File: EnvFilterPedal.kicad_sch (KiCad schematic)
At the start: 114 parts, among them J101 ScopeGroundLoop, J102 IO, Q101 BC857, Q102 BC857, Q103 BC847, U101 TL074, U102 TL074, U103 TL074, U104 LM13700, U105 AZ34063U

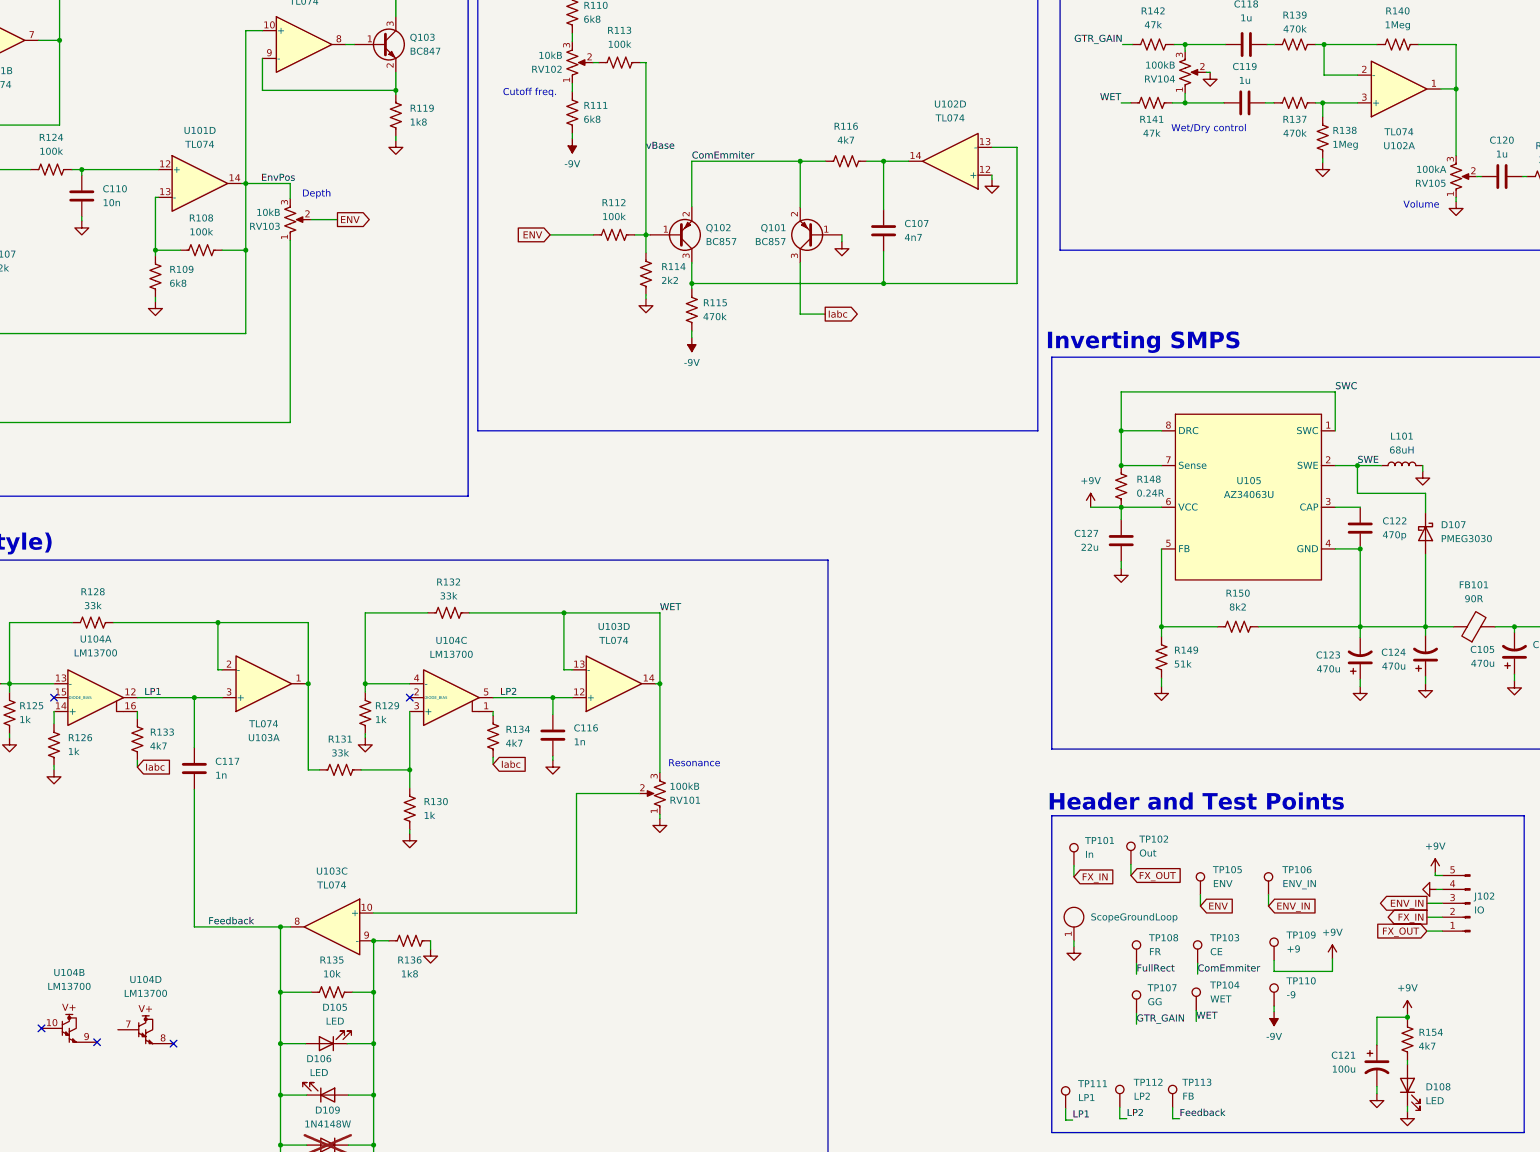
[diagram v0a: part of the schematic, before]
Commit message: component tweaks after playing thru it for a day
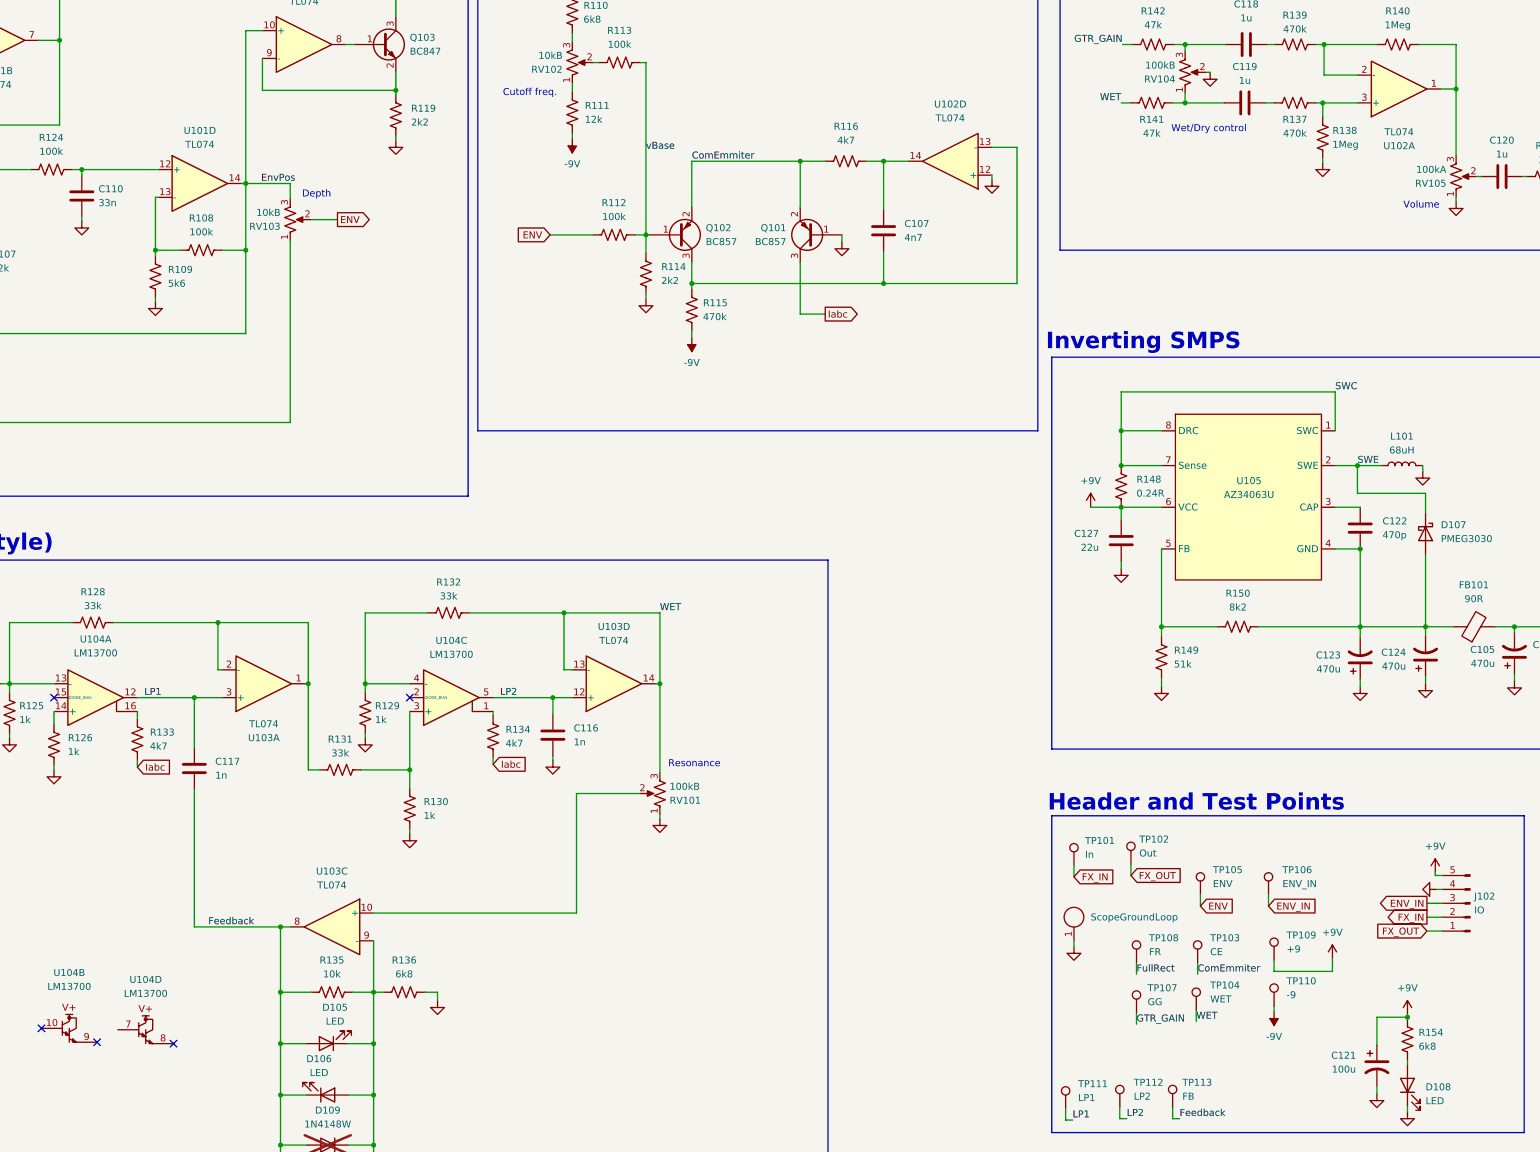
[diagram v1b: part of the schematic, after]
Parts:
- C110: value 10n -> 33n
- R109: value 6k8 -> 5k6
- R111: value 6k8 -> 12k
- R119: value 1k8 -> 2k2
- R136: value 1k8 -> 6k8
- R154: value 4k7 -> 6k8
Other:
- moved on the sheet: R136
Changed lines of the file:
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@@
 	)
 	(junction
-		(at 164.592 214.884)
-		(diameter 0)
-		(color 0 0 0 0)
-	)
-	(junction
 		(at 338.074 61.722)
 		(diameter 0)
@@
 	(wire
 		(pts
+			(xy 164.592 224.282) (xy 166.37 224.282)
+		)
+		(stroke
+			(width 0)
+			(type default)
+		)
+	)
+	(wire
+		(pts
 			(xy 163.068 167.894) (xy 163.068 169.418)
 		)
@@
 	(wire
 		(pts
-			(xy 175.006 214.884) (xy 175.006 216.408)
+			(xy 176.276 224.282) (xy 176.276 225.806)
 		)
 		(stroke
@@
 	(wire
 		(pts
+			(xy 176.276 224.282) (xy 173.99 224.282)
+		)
+		(stroke
+			(width 0)
+			(type default)
+		)
+	)
+	(wire
+		(pts
 			(xy 152.654 261.366) (xy 147.574 261.366)
 		)
@@
 	(wire
 		(pts
-			(xy 164.592 214.884) (xy 167.386 214.884)
-		)
-		(stroke
-			(width 0)
-			(type default)
-		)
-	)
-	(wire
-		(pts
 			(xy 327.914 51.054) (xy 329.184 51.054)
 		)
@@
 			)
 		)
-		(property "Value" "4k7"
+		(property "Value" "6k8"
 			(at 355.6 234.1879 0)
 			(effects
@@
 		(fields_autoplaced yes)
 		(property "Reference" "R119"
-			(at 171.196 62.7379 0)
+			(at 171.45 62.7379 0)
 			(effects
 				(font
@@
 			)
 		)
-		(property "Value" "1k8"
-			(at 171.196 65.2779 0)
+		(property "Value" "2k2"
+			(at 171.45 65.2779 0)
 			(effects
 				(font
@@
 		(fields_autoplaced yes)
 		(property "Reference" "R109"
-			(at 127.254 92.2019 0)
+			(at 127 92.2019 0)
 			(effects
 				(font
@@
 			)
 		)
-		(property "Value" "6k8"
-			(at 127.254 94.7419 0)
+		(property "Value" "5k6"
+			(at 127 94.7419 0)
 			(effects
 				(font
@@
 		(fields_autoplaced yes)
 		(property "Reference" "C110"
-			(at 115.062 77.4699 0)
+			(at 114.3 77.4699 0)
 			(effects
 				(font
@@
 			)
 		)
-		(property "Value" "10n"
-			(at 115.062 80.0099 0)
+		(property "Value" "33n"
+			(at 114.3 80.0099 0)
 			(effects
 				(font
@@
 	(symbol
 		(lib_id "Device:R_US")
-		(at 171.196 214.884 270)
+		(at 170.18 224.282 270)
 		(unit 1)
 		(exclude_from_sim no)
@@
 		(fields_autoplaced yes)
 		(property "Reference" "R136"
-			(at 171.196 218.44 90)
+			(at 170.18 218.44 90)
 			(effects
 				(font
@@
 			)
 		)
-		(property "Value" "1k8"
-			(at 171.196 220.98 90)
+		(property "Value" "6k8"
+			(at 170.18 220.98 90)
 			(effects
 				(font
@@
 		)
 		(property "Footprint" "Resistor_SMD:R_0805_2012Metric"
-			(at 170.942 215.9 90)
+			(at 169.926 225.298 90)
 			(effects
 				(font
@@
 		)
 		(property "Datasheet" "~"
-			(at 171.196 214.884 0)
+			(at 170.18 224.282 0)
 			(effects
 				(font
@@
 		)
 		(property "Description" "Resistor, US symbol"
-			(at 171.196 214.884 0)
+			(at 170.18 224.282 0)
 			(effects
 				(font
@@
 		(fields_autoplaced yes)
 		(property "Reference" "R111"
-			(at 202.946 62.2299 0)
+			(at 203.2 62.2299 0)
 			(effects
 				(font
@@
 			)
 		)
-		(property "Value" "6k8"
-			(at 202.946 64.7699 0)
+		(property "Value" "12k"
+			(at 203.2 64.7699 0)
 			(effects
 				(font
@@
 	(symbol
 		(lib_id "power:GND")
-		(at 175.006 216.408 0)
+		(at 176.276 225.806 0)
 		(mirror y)
 		(unit 1)
@@
 		(fields_autoplaced yes)
 		(property "Reference" "#PWR0141"
-			(at 175.006 222.758 0)
+			(at 176.276 232.156 0)
 			(effects
 				(font
@@
 		)
 		(property "Value" "GND"
-			(at 175.006 220.218 0)
+			(at 176.276 229.616 0)
 			(effects
 				(font
@@
 		)
 		(property "Footprint" ""
-			(at 175.006 216.408 0)
+			(at 176.276 225.806 0)
 			(effects
 				(font
@@
 		)
 		(property "Datasheet" ""
-			(at 175.006 216.408 0)
+			(at 176.276 225.806 0)
 			(effects
 				(font
@@
 		)
 		(property "Description" "Power symbol creates a global label with name \"GND\" , ground"
-			(at 175.006 216.408 0)
+			(at 176.276 225.806 0)
 			(effects
 				(font

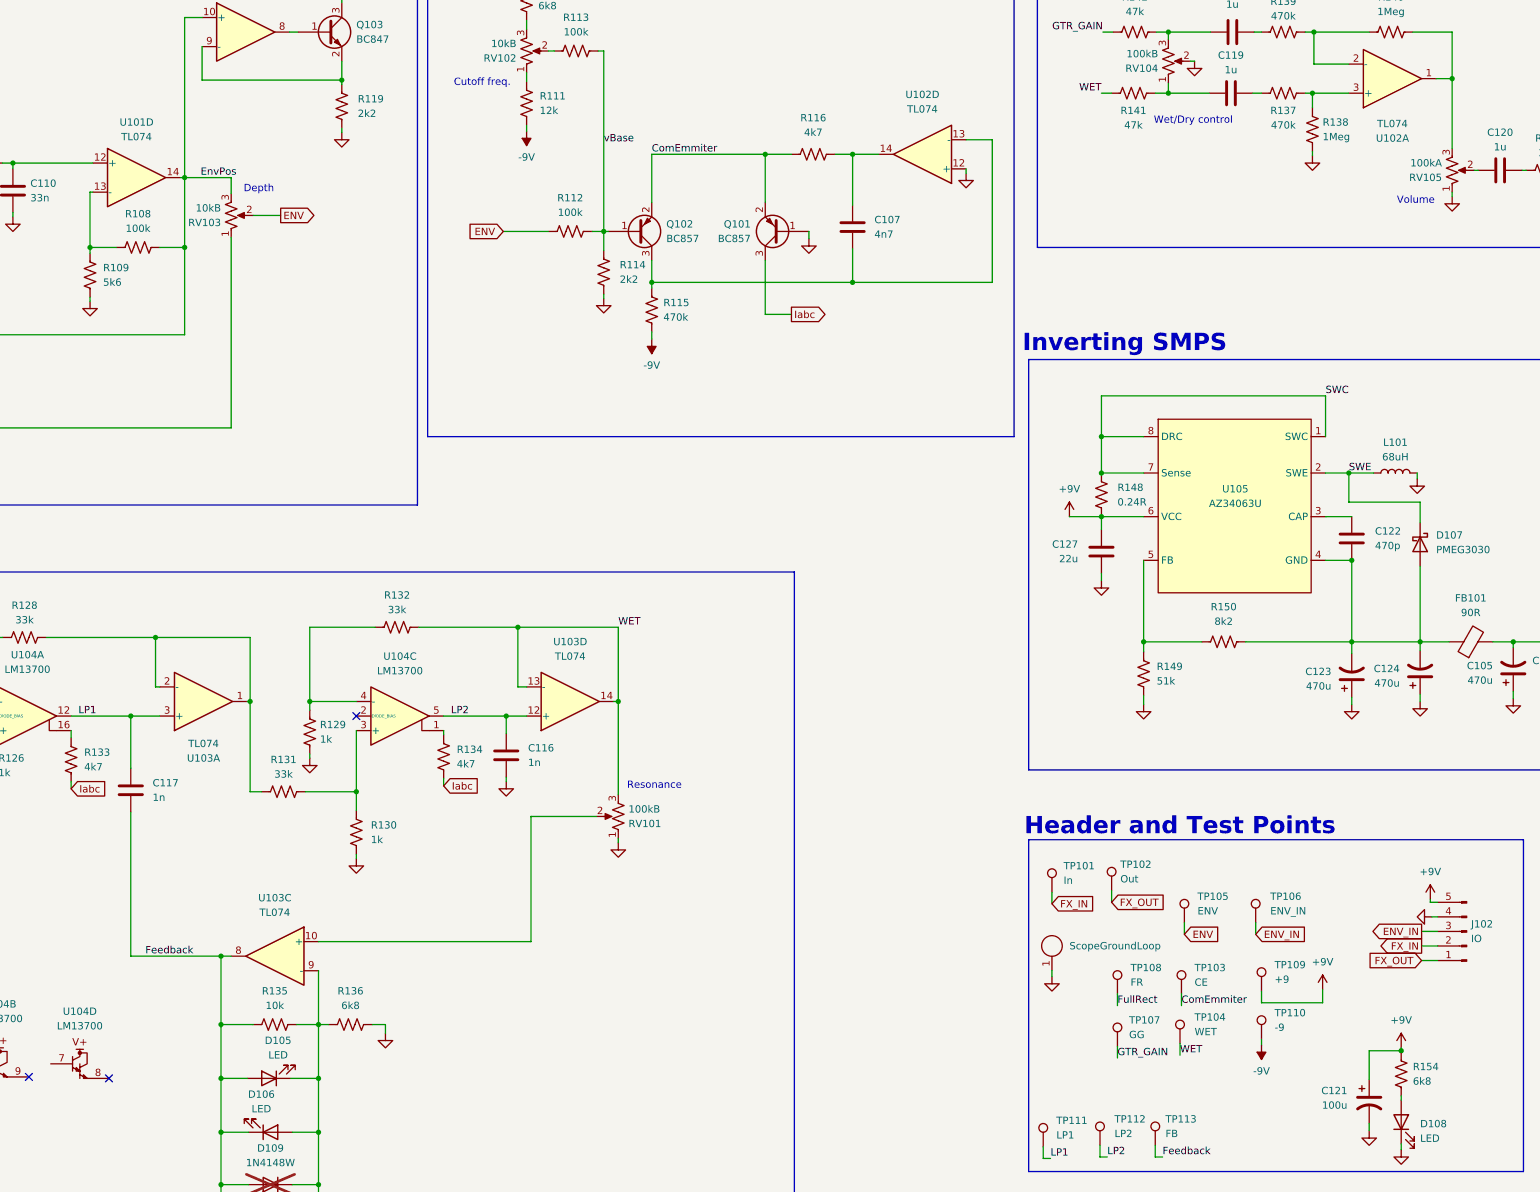
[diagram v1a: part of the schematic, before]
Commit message: minor value tweaks
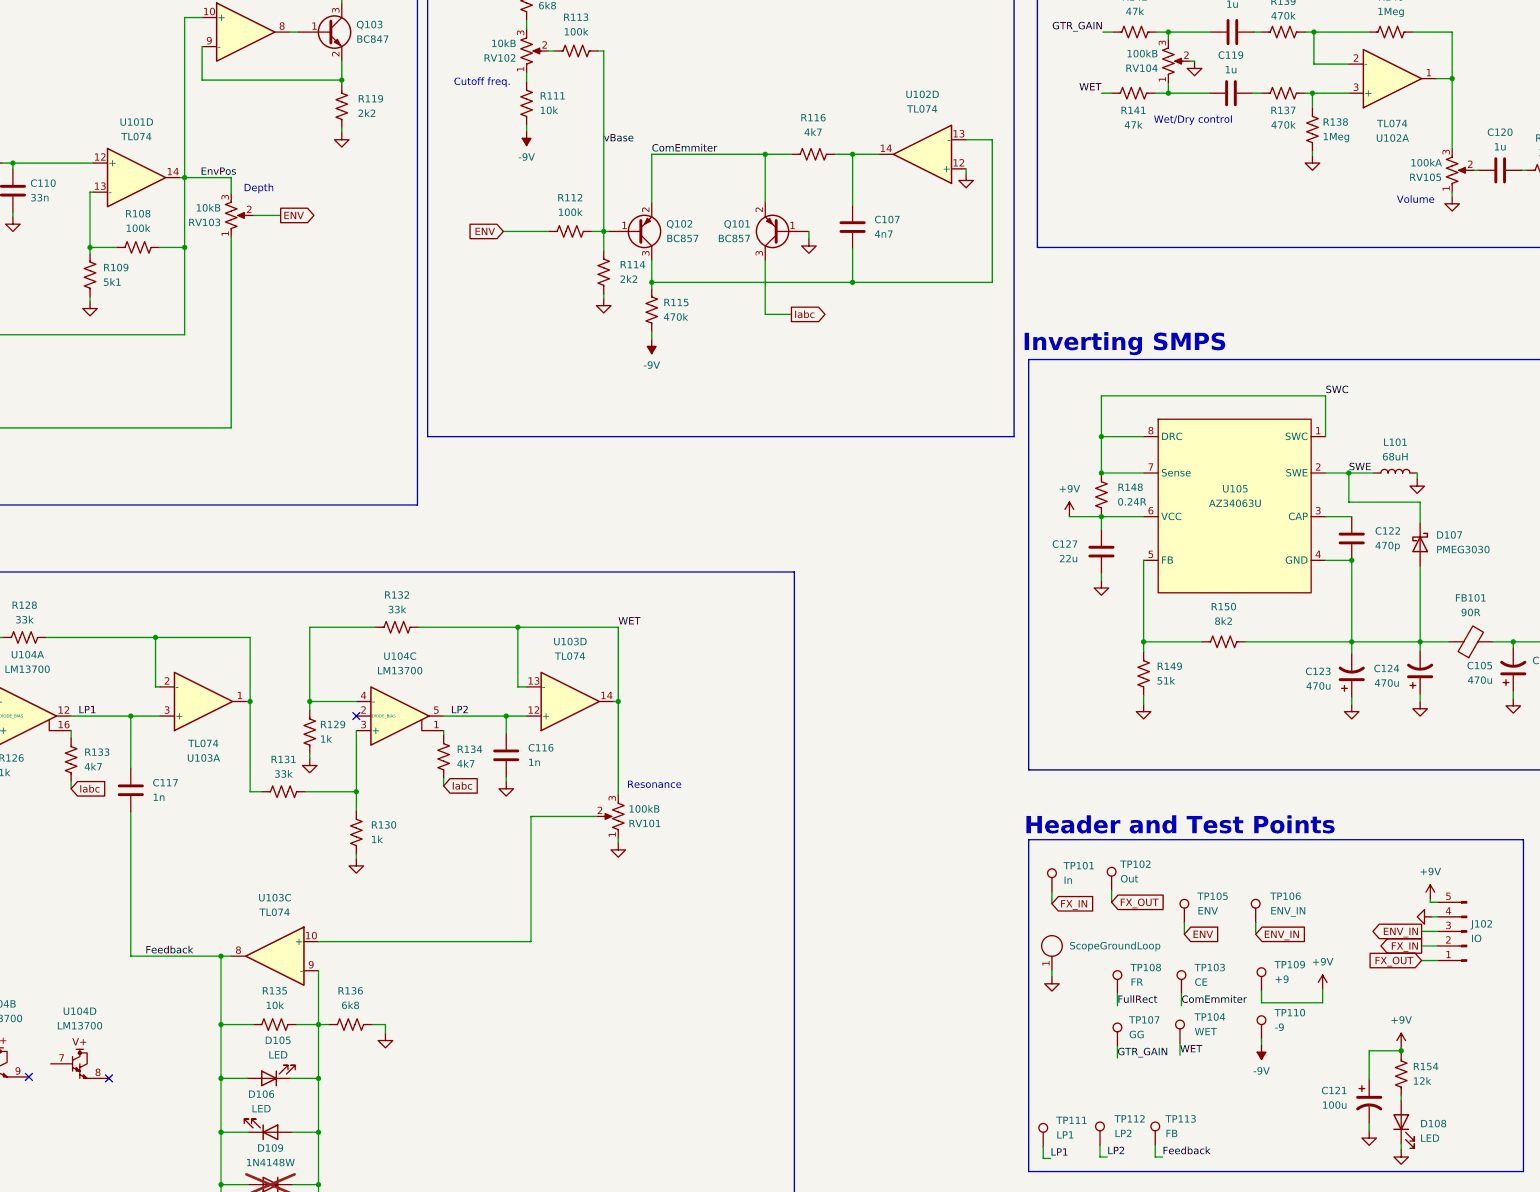
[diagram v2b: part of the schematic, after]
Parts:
- R109: value 5k6 -> 5k1
- R111: value 12k -> 10k
- R154: value 6k8 -> 12k
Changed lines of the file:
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@@
 			)
 		)
-		(property "Value" "6k8"
+		(property "Value" "12k"
 			(at 355.6 234.1879 0)
 			(effects
@@
 			)
 		)
-		(property "Value" "5k6"
+		(property "Value" "5k1"
 			(at 127 94.7419 0)
 			(effects
@@
 			)
 		)
-		(property "Value" "12k"
+		(property "Value" "10k"
 			(at 203.2 64.7699 0)
 			(effects
